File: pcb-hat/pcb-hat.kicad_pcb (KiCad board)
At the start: 4 copper layers, 40.9 x 60.1 mm, 77 parts, among them Q1 Q_PMOS_GSD, Q2 Q_NPN, Q3 PJA3404A_R1_00001, Q4 Q_PMOS_GSD, Q5 Q_NPN, Q6 Q_PMOS_GSD, U1 Headers, U2 HTD Servo, U3 INA219AxD, U4 INA180A1, U5 TL431DBZ, U6 AP63301WU-7, U8 LM3489, U9 Raspberry_Pi_Generic

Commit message: Added bulk capacitor circuit for transmitter, exposed UART pins on Pi for transmitter communication, adjusted silkscreen to accommodate bulk capacitor
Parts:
- added C14: 1000u, Capacitor_SMD:CP_Elec_10x10.5, B.Cu at (120.0, 114.5)
- moved G*** 1.32 mm to (121.7, 97.3)
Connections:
- U9 pad 21: unconnected-(U9-GPIO9/SPI_MISO-Pad21) -> /CAM_RX
- U9 pad 24: unconnected-(U9-GPIO8/~{SPI_CE0}-Pad24) -> /CAM_TX
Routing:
- net +BATT: track 12.4 -> 66.2 mm, vias 3 -> 4

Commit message: Added power circuit for camera transmitter and updated version number on pcb; will resize board and add holes for standoffs soon
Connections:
- C14 pad 1: +BATT -> VCC
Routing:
- net +BATT: track 66.2 -> 25.8 mm, vias 4 -> 3
- net VCC: track 0.00 -> 38.0 mm, vias 15 -> 16
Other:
- board text added: "v0.4"
- board text removed: "v0.3"
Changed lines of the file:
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@@
 			(layers "B.Cu" "B.Mask" "B.Paste")
 			(roundrect_rratio 0.1)
-			(net "+BATT")
+			(net "VCC")
 			(pintype "passive")
 		)
@@
 		)
 	)
-	(gr_text "v0.3"
+	(gr_text "v0.4\n"
 		(at 112.87 121.88 0)
 		(layer "F.SilkS")
@@
 		)
 	)
-	(gr_text "Buzzer: GPIO 5 ▲\nServo: GPIO 26 ▲"
-		(at 126.77 107 270)
+	(gr_text "I2C\n0x40"
+		(at 132.18 74.08 -0)
 		(layer "B.SilkS")
 		(effects
 			(font
-				(size 0.8 0.8)
+				(size 1 1)
 				(thickness 0.2)
 				(bold yes)
 			)
-			(justify left bottom mirror)
+			(justify bottom mirror)
 		)
 	)
-	(gr_text "I2C\n0x40"
-		(at 132.18 74.08 -0)
+	(gr_text "Buzzer: GPIO 5 ▲\nServo: GPIO 26 ▲"
+		(at 126.77 107 270)
 		(layer "B.SilkS")
 		(effects
@@
 				(bold yes)
 			)
-			(justify bottom mirror)
+			(justify left bottom mirror)
 		)
 	)
@@
 		(net "+BATT")
 	)
-	(via
-		(at 118 112.5)
-		(size 0.4)
-		(drill 0.3)
-		(layers "F.Cu" "B.Cu")
-		(net "+BATT")
-	)
-	(segment
-		(start 124.2 114.5)
-		(end 123.2 113.5)
-		(width 0.2)
-		(layer "B.Cu")
-		(net "+BATT")
-	)
 	(segment
 		(start 114.06 65.05)
@@
 	)
 	(segment
-		(start 123.2 113.5)
-		(end 119 113.5)
-		(width 0.2)
-		(layer "B.Cu")
-		(net "+BATT")
-	)
-	(segment
 		(start 119.935 66.14)
 		(end 119.935 64.465)
@@
 	)
 	(segment
-		(start 119 113.5)
-		(end 118 112.5)
-		(width 0.2)
-		(layer "B.Cu")
-		(net "+BATT")
-	)
-	(segment
-		(start 118 112.5)
-		(end 118 79.190466)
-		(width 0.2)
-		(layer "In1.Cu")
-		(net "+BATT")
-	)
-	(segment
 		(start 112.407499 73.597965)
 		(end 112.407499 68.132501)
@@
 	)
 	(via
+		(at 118 112.5)
+		(size 0.4)
+		(drill 0.3)
+		(layers "F.Cu" "B.Cu")
+		(net "VCC")
+	)
+	(via
 		(at 125.72 69.75)
 		(size 0.4)
@@
 	)
 	(segment
+		(start 124.2 114.5)
+		(end 123.2 113.5)
+		(width 0.2)
+		(layer "B.Cu")
+		(net "VCC")
+	)
+	(segment
+		(start 123.2 113.5)
+		(end 119 113.5)
+		(width 0.2)
+		(layer "B.Cu")
+		(net "VCC")
+	)
+	(segment
+		(start 119 113.5)
+		(end 118 112.5)
+		(width 0.2)
+		(layer "B.Cu")
+		(net "VCC")
+	)
+	(segment
+		(start 118 112.5)
+		(end 118 82.78)
+		(width 0.2)
+		(layer "In2.Cu")
+		(net "VCC")
+	)
+	(segment
+		(start 118 82.78)
+		(end 118.91 81.87)
+		(width 0.2)
+		(layer "In2.Cu")
+		(net "VCC")
+	)
+	(segment
 		(start 115.815 77.39)
 		(end 114.3125 77.39)
@@
 			)
 		)
+	)
+	(zone
+		(net "VCC")
+		(layer "In2.Cu")
+		(hatch none 0.1)
+		(priority 30007)
+		(attr
+			(teardrop
+				(type padvia)
+			)
+		)
+		(connect_pads yes
+			(clearance 0)
+		)
+		(min_thickness 0.0254)
+		(fill yes
+			(island_removal_mode 1)
+		)
+		(polygon
+			(pts
+				(xy 118.53088 82.107698) (xy 118.672302 82.24912) (xy 119.021114 82.036294) (xy 118.913424 81.866576)
+				(xy 118.743706 81.758886)
+			)
+		)

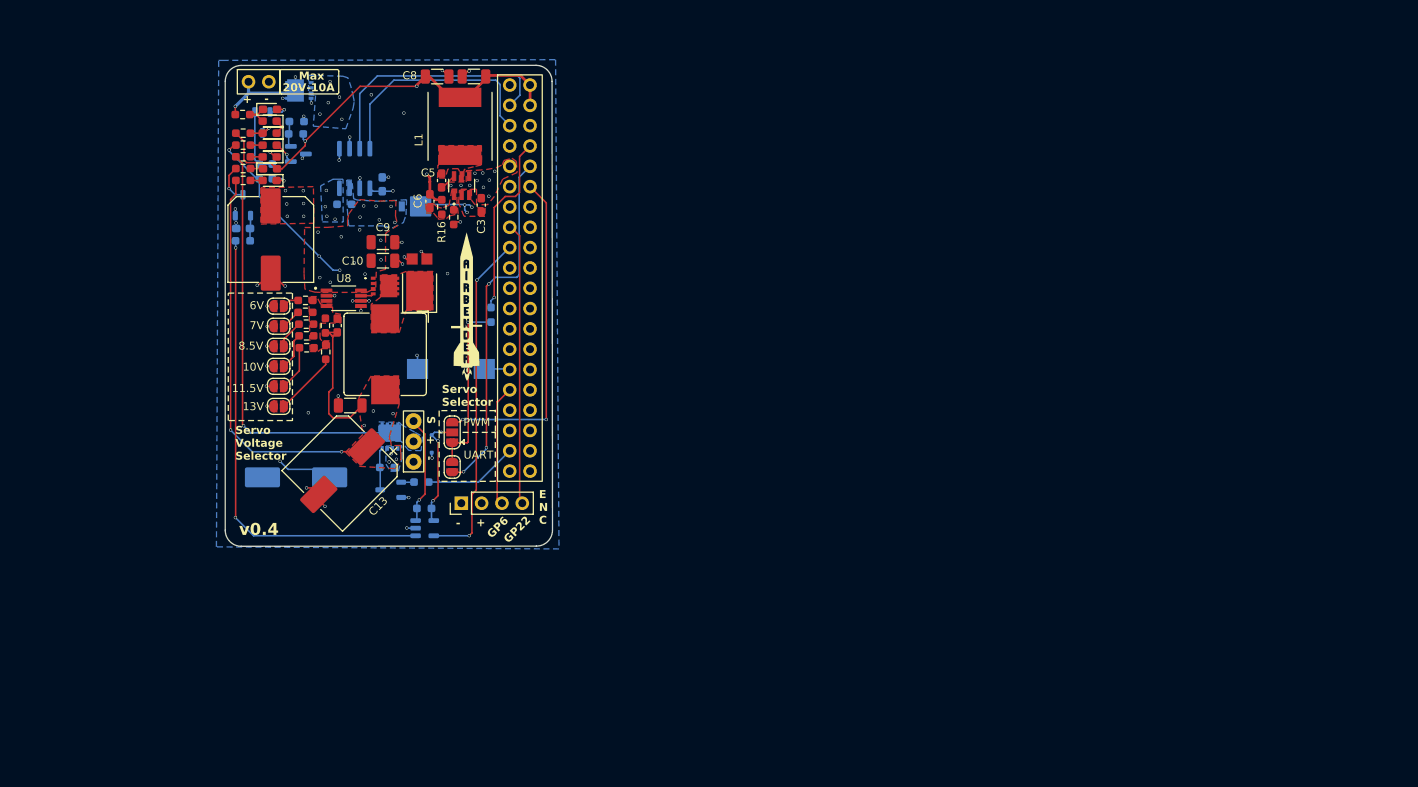
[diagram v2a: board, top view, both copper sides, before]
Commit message: started new pcb layout; added mounting holes for standoffs and redid pcb edge cuts
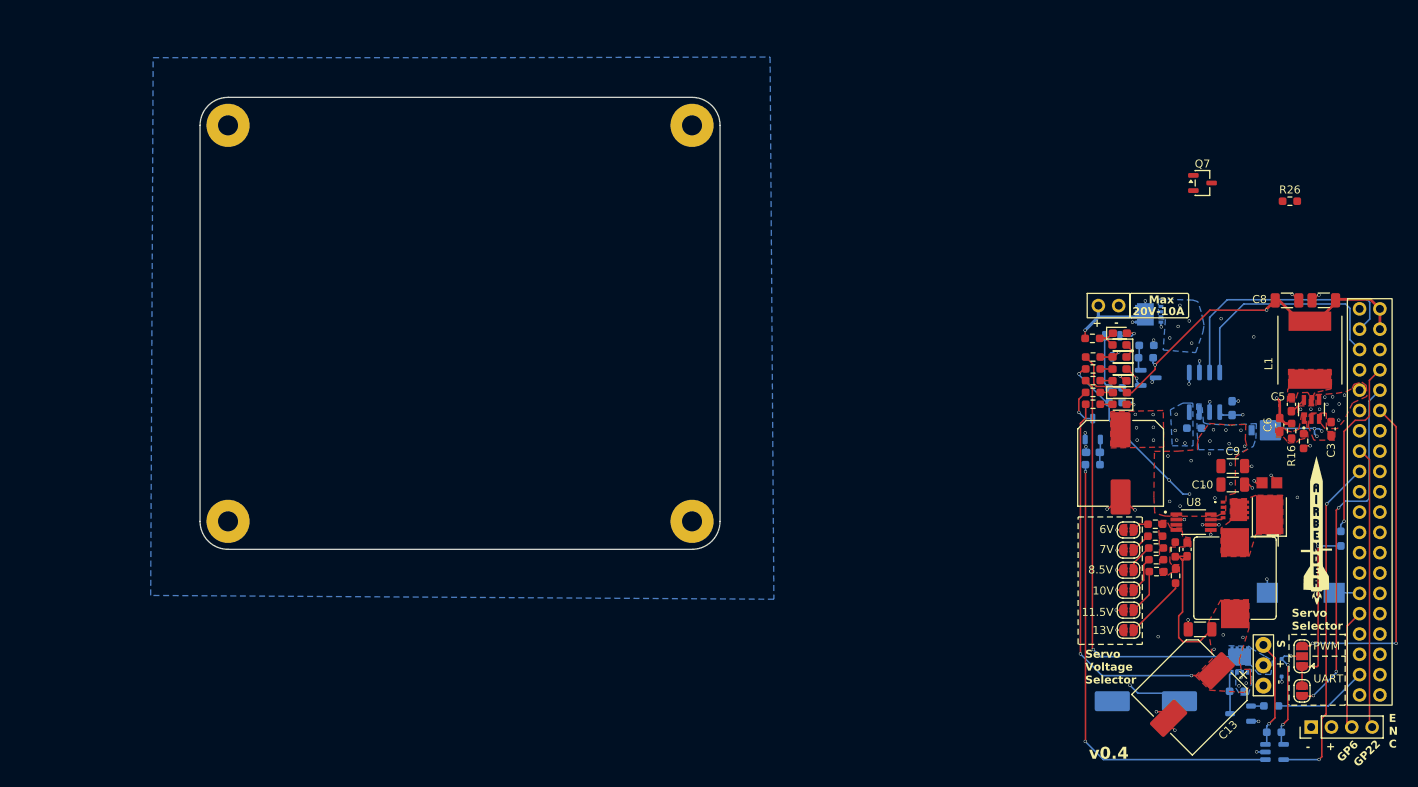
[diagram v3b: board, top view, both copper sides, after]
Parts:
- added H1: MountingHole_Pad, Module:Maple_Mini, F.Cu at (111.5, 70.5)
- added H2: MountingHole_Pad, Module:Maple_Mini, F.Cu at (169.5, 70.5)
- added H3: MountingHole_Pad, Module:Maple_Mini, F.Cu at (111.5, 120.0)
- added H4: MountingHole_Pad, Module:Maple_Mini, F.Cu at (169.5, 120.0)
- added Q7: NMOS, Package_TO_SOT_SMD:SOT-23-3, F.Cu at (233.3, 77.7)
- added R26: 10k, Resistor_SMD:R_0603_1608Metric_Pad0.98x0.95mm_HandSolder, F.Cu at (244.2, 80.0)
- moved C4 109.9 mm to (219.6, 111.4)
- moved C6 109.9 mm to (243.0, 108.0)
- moved C8 109.9 mm to (243.9, 92.4)
- moved G*** 109.9 mm to (247.5, 124.9)
- moved L2 109.9 mm to (237.4, 127.1)
- moved R1 109.9 mm to (232.3, 108.3)
- moved R11 109.9 mm to (219.6, 112.9)
- moved R13 109.9 mm to (237.6, 141.2)
- moved R2 109.9 mm to (219.6, 97.1)
- moved U5 109.9 mm to (226.5, 102.1)
- moved U6 109.9 mm to (246.9, 106.0)
- moved U9 109.9 mm to (254.2, 117.4)
- moved C12 109.9 mm to (233.0, 133.5)
- moved C13 109.9 mm to (232.0, 141.6)
- moved D2 109.9 mm to (222.9, 98.0)
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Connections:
- U9 pad 32: unconnected-(U9-GPIO12-Pad32) -> /FAN_NMOS
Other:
- board size 40.9 x 60.1 mm -> 65 x 56.5 mm

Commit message: Lots of progress on layout; routing is kinda shit and drc is complaining about a lot, im tired now so ill fix it later
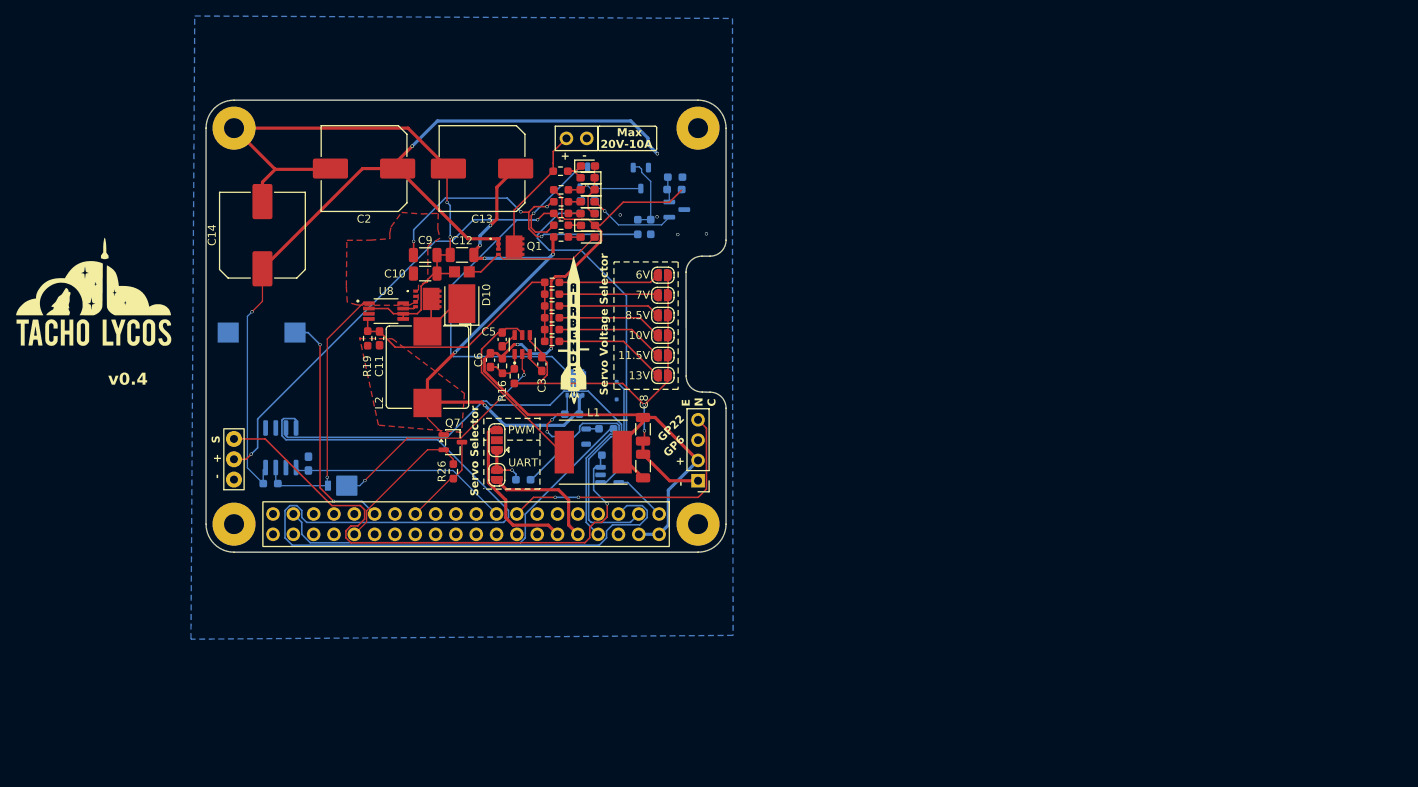
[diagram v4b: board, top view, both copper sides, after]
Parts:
- C14, G***, Q1: moved to F.Cu
- moved G*** 138.2 mm to (94.7, 88.6), turned to 0 degrees
- moved LS1 133.9 mm to (115.7, 96.4)
- moved U2 131.2 mm to (112.2, 112.2)
- moved C14 124.9 mm to (115.8, 84.2), turned to 90 degrees
- moved R1 115.7 mm to (116.8, 115.3)
- moved U3 115.7 mm to (118.1, 110.8)
- moved C1 115.7 mm to (121.5, 112.8)
- moved D5 115.7 mm to (125.6, 115.5)
- moved U9 112.8 mm to (141.4, 120.3), turned to -90 degrees
- moved C13 110.5 mm to (143.2, 75.9), turned to 180 degrees
- moved R26 109.9 mm to (139.7, 113.8), turned to 90 degrees
- moved C10 104.3 mm to (136.1, 89.0)
- moved C11 104.3 mm to (130.4, 97.1)
- moved C9 104.3 mm to (136.1, 86.7)
- moved D10 104.3 mm to (140.7, 91.7)
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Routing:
- net GND: track 46.9 -> 187.6 mm, vias 53 -> 8
- net VCC: track 38.0 -> 138.9 mm, vias 16 -> 3
- net /PI_SCL: track 28.9 -> 123.9 mm
- net /SERVO_SIGNAL: track 13.1 -> 69.2 mm
- net VCC_LOAD: track 22.0 -> 73.5 mm, vias 18 -> 5
- net +5V: track 130.2 -> 176.0 mm, vias 3 -> 2
- net /SERVO_SWITCH: track 52.7 -> 95.6 mm, vias 1 -> 2
- net /GPIO26: track 11.8 -> 50.0 mm
- net /PI_SDA: track 31.8 -> 68.5 mm
- net /V_CHOOSE: track 0.00 -> 35.3 mm
- net /GPIO6: track 15.1 -> 46.8 mm
- net /PI_RX_OUT: track 44.6 -> 14.8 mm, vias 3 -> 0
- net +3V3: track 85.3 -> 56.2 mm, vias 3 -> 0
- net /GPIO5: track 3.11 -> 29.8 mm, vias 0 -> 2
- net Net-(D5-K): track 7.73 -> 34.3 mm
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- added copper zone on In2.Cu, net +5V
- removed copper zone on B.Cu, net /SERVO_SWITCH
- removed copper zone on F.Cu, net /V_CHOOSE
- removed copper zone on F.Cu, net GND
- removed copper zone on F.Cu, net Net-(D10-K)
- removed copper zone on F.Cu, net Net-(D5-K)
- removed copper zone on F.Cu, net Net-(U6-FB)
- removed copper zone on F.Cu, net Net-(U6-SW)
- removed copper zone on B.Cu, net VCC
- removed copper zone on F.Cu, net VCC
- removed copper zone on B.Cu, net VCC_LOAD
- removed copper zone on B.Cu, net VDC
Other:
- outline, holes or cut-outs redrawn
